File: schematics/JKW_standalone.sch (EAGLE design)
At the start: 229 parts, among them IC1 4093D, IC4 ATMEGA2560-16AU, Q1 BSS84, Q10 BSS84, Q11 BSS84, Q2 BSS84, Q3 BSS84, Q4 BSS84, Q5 BSS84, Q6 BSS84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

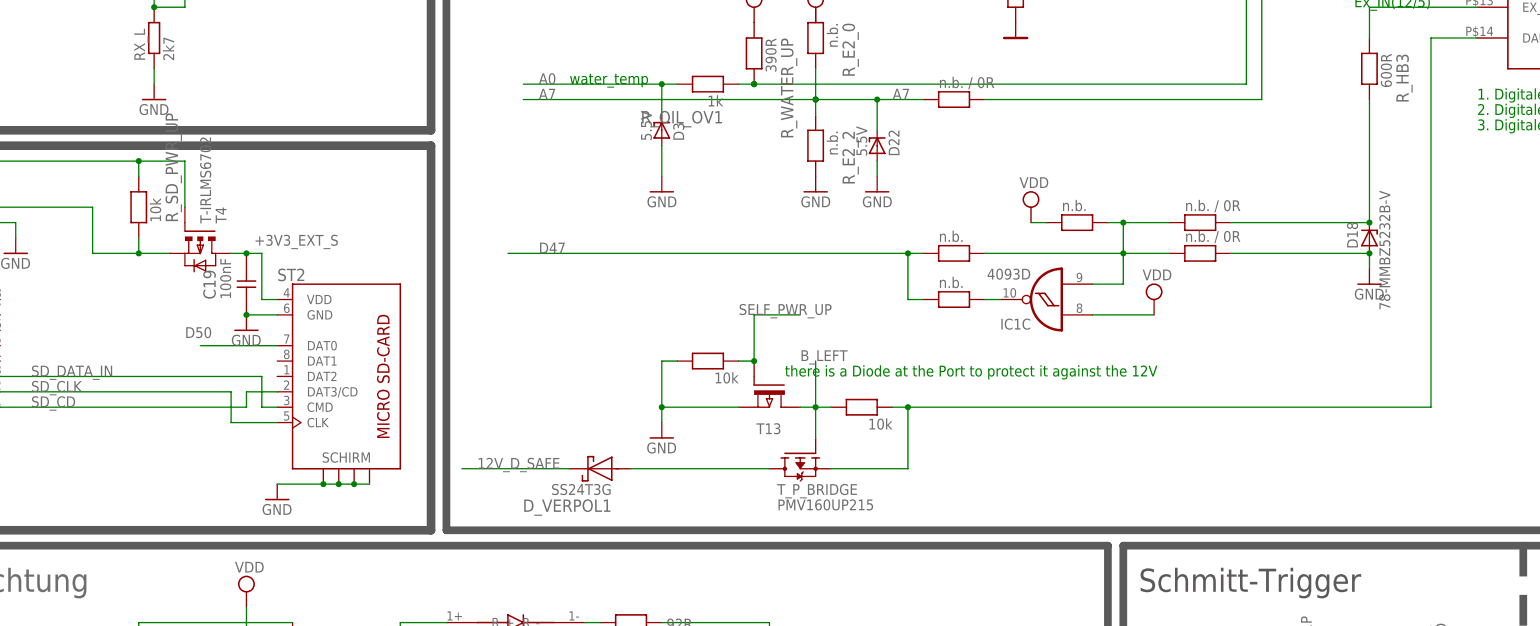
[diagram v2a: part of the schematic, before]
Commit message: improved wiring
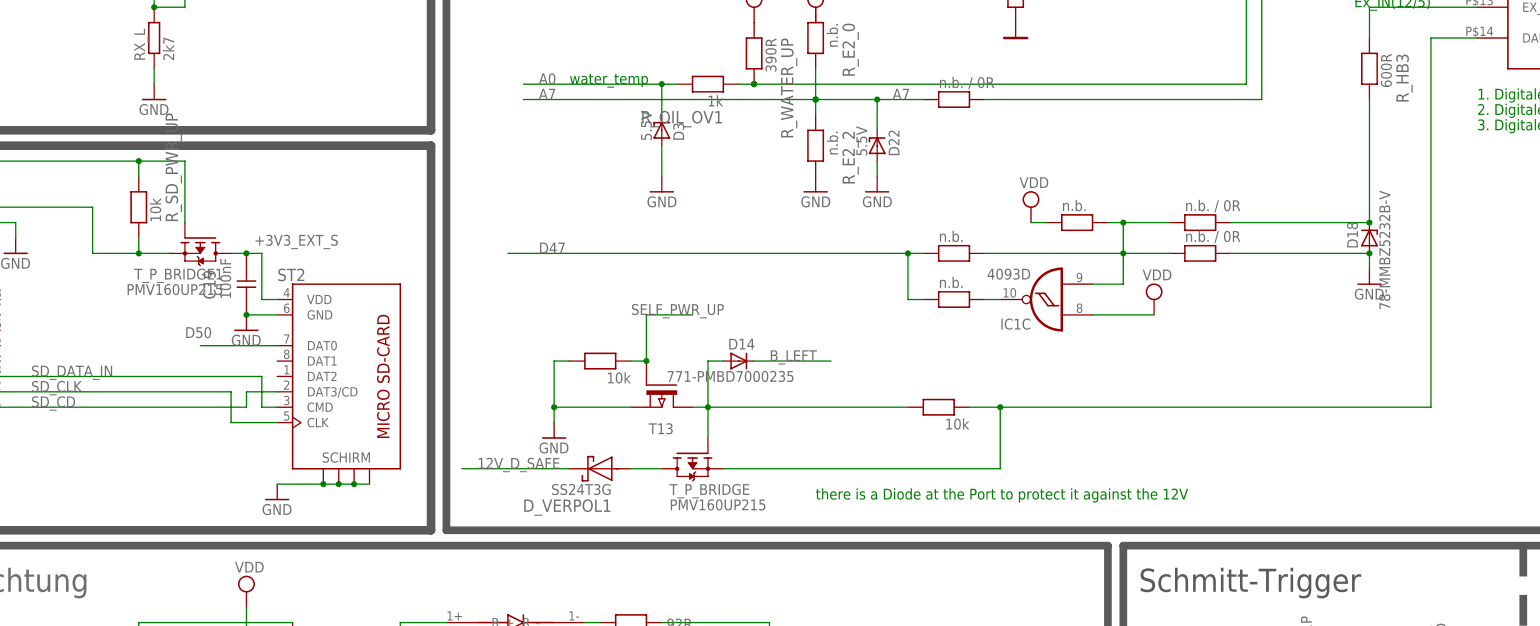
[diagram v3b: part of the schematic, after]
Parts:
- removed T4: T-IRLMS6702, RCLDT:T-IRLMS6702
- added D14: 771-PMBD7000235, semicon-smd-ipc:D-A1-C3
- added T_P_BRIDGE1: PMV160UP215, Kolja:PMV160UP215
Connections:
- new net NET12: D14.A, R_DEAKT_DAUER_P.2, T13.D, T_P_BRIDGE.G
- net +3V3_EXT: now also T_P_BRIDGE1.S; no longer T4.S
- net +3V3_EXT_S: now also T_P_BRIDGE1.D; no longer T4.D1, T4.D2, T4.D3, T4.D4
- net B_LEFT: now also D14.C; no longer R_DEAKT_DAUER_P.2, T13.D, T_P_BRIDGE.G
- net D4: now also T_P_BRIDGE1.G; no longer T4.G
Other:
- moved on the sheet: T13, T_P_BRIDGE
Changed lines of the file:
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@@
 <part name="R_TX_UP" library="RCLDT" deviceset="R" device="0805" value="1k2"/>
 <part name="JP2" library="pinhead" deviceset="PINHD-2X3" device="" value="ICSP"/>
-<part name="T4" library="RCLDT" deviceset="T-IRLMS6702" device=""/>
 <part name="T5" library="RCLDT" deviceset="T-P-FET" device="BSS139" value="Mouser: 771-2N7002BK215 , N-Channel, 60V 350mA, SOT-23, 0,052€"/>
 <part name="GND10" library="supply1" deviceset="GND" device=""/>
@@
 <part name="T_P_BRIDGE" library="Kolja" deviceset="PMV160UP215" device=""/>
 <part name="TX2" library="pinhead" deviceset="PINHD-1X2" device=""/>
+<part name="T_P_BRIDGE1" library="Kolja" deviceset="PMV160UP215" device=""/>
+<part name="D14" library="semicon-smd-ipc" deviceset="D-" device="A1-C3" value="771-PMBD7000235"/>
 </parts>
 <sheets>
@@
 <text x="-137.16" y="-15.24" size="1.778" layer="91">Bluetooth toggle</text>
 <text x="-144.78" y="-20.32" size="1.778" layer="91">V meas</text>
-<text x="71.12" y="91.44" size="1.778" layer="91">there is a Diode at the Port to protect it against the 12V</text>
+<text x="76.2" y="71.12" size="1.778" layer="91">there is a Diode at the Port to protect it against the 12V</text>
 </plain>
 <instances>
@@
 </instance>
 <instance part="JP2" gate="A" x="-132.08" y="38.1" rot="R90"/>
-<instance part="T4" gate="G$1" x="-25.4" y="114.3" rot="MR270"/>
 <instance part="T5" gate="G$1" x="274.32" y="111.76" rot="MR270"/>
 <instance part="GND10" gate="1" x="358.14" y="226.06"/>
@@
 <attribute name="VALUE" x="42.545" y="73.66" size="1.778" layer="96" rot="R180"/>
 </instance>
-<instance part="R_DEAKT_DAUER_P" gate="G$1" x="83.82" y="86.36" smashed="yes" rot="R180">
-<attribute name="VALUE" x="88.9" y="84.455" size="1.778" layer="96" rot="R180"/>
+<instance part="R_DEAKT_DAUER_P" gate="G$1" x="96.52" y="86.36" smashed="yes" rot="R180">
+<attribute name="VALUE" x="101.6" y="84.455" size="1.778" layer="96" rot="R180"/>
 </instance>
-<instance part="T13" gate="G$1" x="68.58" y="88.9" smashed="yes" rot="MR270">
-<attribute name="NAME" x="66.421" y="81.915" size="1.778" layer="95"/>
+<instance part="T13" gate="G$1" x="50.8" y="88.9" smashed="yes" rot="MR270">
+<attribute name="NAME" x="48.641" y="81.915" size="1.778" layer="95"/>
 </instance>
-<instance part="GND15" gate="1" x="50.8" y="81.28"/>
-<instance part="R_DEAKT_DAUER_P1" gate="G$1" x="58.42" y="93.98" smashed="yes" rot="R180">
-<attribute name="VALUE" x="63.5" y="92.075" size="1.778" layer="96" rot="R180"/>
+<instance part="GND15" gate="1" x="33.02" y="81.28"/>
+<instance part="R_DEAKT_DAUER_P1" gate="G$1" x="40.64" y="93.98" smashed="yes" rot="R180">
+<attribute name="VALUE" x="45.72" y="92.075" size="1.778" layer="96" rot="R180"/>
 </instance>
 <instance part="D12" gate="G$1" x="-261.62" y="121.92" smashed="yes" rot="R180"/>
-<instance part="T_P_BRIDGE" gate="G$1" x="73.66" y="78.74" smashed="yes" rot="MR270">
-<attribute name="VALUE" x="69.85" y="71.12" size="1.778" layer="96" rot="MR180"/>
-<attribute name="NAME" x="69.85" y="73.66" size="1.778" layer="95" rot="MR180"/>
+<instance part="T_P_BRIDGE" gate="G$1" x="55.88" y="78.74" smashed="yes" rot="MR270">
+<attribute name="VALUE" x="52.07" y="71.12" size="1.778" layer="96" rot="MR180"/>
+<attribute name="NAME" x="52.07" y="73.66" size="1.778" layer="95" rot="MR180"/>
 </instance>
 <instance part="TX2" gate="G$1" x="-287.02" y="144.78"/>
+<instance part="T_P_BRIDGE1" gate="G$1" x="-25.4" y="114.3" smashed="yes" rot="R270">
+<attribute name="VALUE" x="-21.59" y="106.68" size="1.778" layer="96" rot="R180"/>
+<attribute name="NAME" x="-21.59" y="109.22" size="1.778" layer="95" rot="R180"/>
+</instance>
+<instance part="D14" gate="G$1" x="63.5" y="93.98" smashed="yes">
+<attribute name="NAME" x="61.722" y="95.885" size="1.778" layer="95"/>
+<attribute name="VALUE" x="51.562" y="90.551" size="1.778" layer="96"/>
+</instance>
 </instances>
 <busses>
@@
 <pinref part="GND15" gate="1" pin="GND"/>
 <pinref part="T13" gate="G$1" pin="S"/>
-<wire x1="50.8" y1="83.82" x2="50.8" y2="86.36" width="0.1524" layer="91"/>
-<wire x1="50.8" y1="86.36" x2="63.5" y2="86.36" width="0.1524" layer="91"/>
+<wire x1="33.02" y1="83.82" x2="33.02" y2="86.36" width="0.1524" layer="91"/>
+<wire x1="33.02" y1="86.36" x2="45.72" y2="86.36" width="0.1524" layer="91"/>
 <pinref part="R_DEAKT_DAUER_P1" gate="G$1" pin="2"/>
-<wire x1="50.8" y1="86.36" x2="50.8" y2="93.98" width="0.1524" layer="91"/>
-<wire x1="50.8" y1="93.98" x2="53.34" y2="93.98" width="0.1524" layer="91"/>
-<junction x="50.8" y="86.36"/>
+<wire x1="33.02" y1="86.36" x2="33.02" y2="93.98" width="0.1524" layer="91"/>
+<wire x1="33.02" y1="93.98" x2="35.56" y2="93.98" width="0.1524" layer="91"/>
+<junction x="33.02" y="86.36"/>
 </segment>
 </net>
@@
 <wire x1="-35.56" y1="114.3" x2="-35.56" y2="111.76" width="0.1524" layer="91"/>
 <junction x="-35.56" y="111.76"/>
-<pinref part="T4" gate="G$1" pin="S"/>
 <pinref part="R_SD_PWR_UP" gate="G$1" pin="1"/>
 <wire x1="-43.18" y1="111.76" x2="-43.18" y2="119.38" width="0.1524" layer="91"/>
@@
 <wire x1="-71.12" y1="119.38" x2="-71.12" y2="116.84" width="0.1524" layer="91"/>
 <wire x1="-71.12" y1="116.84" x2="-73.66" y2="116.84" width="0.1524" layer="91"/>
+<pinref part="T_P_BRIDGE1" gate="G$1" pin="S"/>
 </segment>
 </net>
@@
 </segment>
 <segment>
-<wire x1="-27.94" y1="119.38" x2="-27.94" y2="127" width="0.1524" layer="91"/>
+<wire x1="-27.94" y1="116.84" x2="-27.94" y2="127" width="0.1524" layer="91"/>
 <wire x1="-27.94" y1="127" x2="-35.56" y2="127" width="0.1524" layer="91"/>
 <wire x1="-35.56" y1="127" x2="-86.36" y2="127" width="0.1524" layer="91"/>
@@
 <junction x="-35.56" y="127"/>
 <label x="-86.36" y="127" size="1.778" layer="95"/>
-<pinref part="T4" gate="G$1" pin="G"/>
 <pinref part="R_SD_PWR_UP" gate="G$1" pin="2"/>
+<pinref part="T_P_BRIDGE1" gate="G$1" pin="G"/>
 </segment>
 </net>
@@
 <pinref part="ST2" gate="G$1" pin="VDD"/>
 <pinref part="C19" gate="C" pin="2"/>
-<pinref part="T4" gate="G$1" pin="D1"/>
-<pinref part="T4" gate="G$1" pin="D2"/>
-<pinref part="T4" gate="G$1" pin="D3"/>
-<pinref part="T4" gate="G$1" pin="D4"/>
+<pinref part="T_P_BRIDGE1" gate="G$1" pin="D"/>
 </segment>
 </net>
@@
 </segment>
 <segment>
-<wire x1="76.2" y1="93.98" x2="76.2" y2="86.36" width="0.1524" layer="91"/>
-<label x="73.66" y="93.98" size="1.778" layer="95"/>
-<wire x1="78.74" y1="86.36" x2="76.2" y2="86.36" width="0.1524" layer="91"/>
-<wire x1="76.2" y1="86.36" x2="76.2" y2="81.28" width="0.1524" layer="91"/>
-<pinref part="R_DEAKT_DAUER_P" gate="G$1" pin="2"/>
-<wire x1="76.2" y1="86.36" x2="73.66" y2="86.36" width="0.1524" layer="91"/>
-<junction x="76.2" y="86.36"/>
-<pinref part="T13" gate="G$1" pin="D"/>
-<pinref part="T_P_BRIDGE" gate="G$1" pin="G"/>
-</segment>
-<segment>
 <pinref part="D12" gate="G$1" pin="C"/>
 <wire x1="-264.16" y1="121.92" x2="-274.32" y2="121.92" width="0.1524" layer="91"/>
 <label x="-271.78" y="121.92" size="1.778" layer="95"/>
 </segment>
+<segment>
+<pinref part="D14" gate="G$1" pin="C"/>
+<wire x1="66.04" y1="93.98" x2="78.74" y2="93.98" width="0.1524" layer="91"/>
+<label x="68.58" y="93.98" size="1.778" layer="95"/>
+</segment>
 </net>
 <net name="B_UP" class="0">
@@
 <pinref part="SPEEDOSTECKER" gate="G$1" pin="DAUER_VIN"/>
 <wire x1="185.42" y1="147.32" x2="177.8" y2="147.32" width="0.1524" layer="91"/>
-<wire x1="78.74" y1="76.2" x2="91.44" y2="76.2" width="0.1524" layer="91"/>
-<wire x1="91.44" y1="76.2" x2="91.44" y2="86.36" width="0.1524" layer="91"/>
+<wire x1="60.96" y1="76.2" x2="106.68" y2="76.2" width="0.1524" layer="91"/>
+<wire x1="106.68" y1="76.2" x2="106.68" y2="86.36" width="0.1524" layer="91"/>
 <pinref part="R_DEAKT_DAUER_P" gate="G$1" pin="1"/>
-<wire x1="88.9" y1="86.36" x2="91.44" y2="86.36" width="0.1524" layer="91"/>
-<junction x="91.44" y="86.36"/>
-<wire x1="91.44" y1="86.36" x2="177.8" y2="86.36" width="0.1524" layer="91"/>
+<wire x1="101.6" y1="86.36" x2="106.68" y2="86.36" width="0.1524" layer="91"/>
+<junction x="106.68" y="86.36"/>
+<wire x1="106.68" y1="86.36" x2="177.8" y2="86.36" width="0.1524" layer="91"/>
 <wire x1="177.8" y1="86.36" x2="177.8" y2="147.32" width="0.1524" layer="91"/>
 <pinref part="T_P_BRIDGE" gate="G$1" pin="S"/>
@@
 <segment>
 <pinref part="D_VERPOL1" gate="G$1" pin="A"/>
-<wire x1="68.58" y1="76.2" x2="45.72" y2="76.2" width="0.1524" layer="91"/>
+<wire x1="50.8" y1="76.2" x2="45.72" y2="76.2" width="0.1524" layer="91"/>
 <pinref part="T_P_BRIDGE" gate="G$1" pin="D"/>
 </segment>
@@
 <pinref part="T13" gate="G$1" pin="G"/>
 <pinref part="R_DEAKT_DAUER_P1" gate="G$1" pin="1"/>
-<wire x1="66.04" y1="93.98" x2="63.5" y2="93.98" width="0.1524" layer="91"/>
-<wire x1="66.04" y1="93.98" x2="66.04" y2="101.6" width="0.1524" layer="91"/>
-<wire x1="66.04" y1="101.6" x2="73.66" y2="101.6" width="0.1524" layer="91"/>
-<junction x="66.04" y="93.98"/>
-<label x="63.5" y="101.6" size="1.778" layer="95"/>
+<wire x1="48.26" y1="93.98" x2="45.72" y2="93.98" width="0.1524" layer="91"/>
+<wire x1="48.26" y1="93.98" x2="48.26" y2="101.6" width="0.1524" layer="91"/>
+<wire x1="48.26" y1="101.6" x2="55.88" y2="101.6" width="0.1524" layer="91"/>
+<junction x="48.26" y="93.98"/>
+<label x="45.72" y="101.6" size="1.778" layer="95"/>
 </segment>
 <segment>
@@
 </segment>
 </net>
+<net name="NET12" class="0">
+<segment>
+<wire x1="58.42" y1="93.98" x2="58.42" y2="86.36" width="0.1524" layer="91"/>
+<wire x1="91.44" y1="86.36" x2="58.42" y2="86.36" width="0.1524" layer="91"/>
+<wire x1="58.42" y1="86.36" x2="58.42" y2="81.28" width="0.1524" layer="91"/>
+<pinref part="R_DEAKT_DAUER_P" gate="G$1" pin="2"/>
+<wire x1="58.42" y1="86.36" x2="55.88" y2="86.36" width="0.1524" layer="91"/>
+<junction x="58.42" y="86.36"/>
+<pinref part="T13" gate="G$1" pin="D"/>
+<pinref part="T_P_BRIDGE" gate="G$1" pin="G"/>
+<pinref part="D14" gate="G$1" pin="A"/>
+<wire x1="60.96" y1="93.98" x2="58.42" y2="93.98" width="0.1524" layer="91"/>
+</segment>
+</net>

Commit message: Added Capacitor to Display and sandboxed HF-Parts
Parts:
- added C10, C12, C13, GPS_C5: 100nF, RCLDT:C0805
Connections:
- net +3V3_EXT: now also C10.2, C12.2, C13.2, GPS_C5.2
- net GND: now also C10.1, C12.1, C13.1, GPS_C5.1
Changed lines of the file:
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@@
 <?xml version="1.0" encoding="utf-8"?>
 <!DOCTYPE eagle SYSTEM "eagle.dtd">
-<eagle version="6.2">
+<eagle version="6.1">
 <drawing>
 <settings>
@@
 <part name="T_P_BRIDGE1" library="Kolja" deviceset="PMV160UP215" device=""/>
 <part name="D14" library="semicon-smd-ipc" deviceset="D-" device="A1-C3" value="771-PMBD7000235"/>
+<part name="GPS_C5" library="RCLDT" deviceset="C" device="0805" value="100nF"/>
+<part name="C10" library="RCLDT" deviceset="C" device="0805" value="100nF"/>
+<part name="C12" library="RCLDT" deviceset="C" device="0805" value="100nF"/>
+<part name="C13" library="RCLDT" deviceset="C" device="0805" value="100nF"/>
 </parts>
 <sheets>
@@
 <attribute name="VALUE" x="51.562" y="90.551" size="1.778" layer="96"/>
 </instance>
+<instance part="GPS_C5" gate="C" x="236.22" y="162.56" smashed="yes" rot="R90">
+<attribute name="NAME" x="238.76" y="165.1" size="2.032" layer="95" rot="R90"/>
+<attribute name="VALUE" x="233.68" y="160.02" size="1.778" layer="96" rot="R90"/>
+</instance>
+<instance part="C10" gate="C" x="-312.42" y="50.8" rot="R270"/>
+<instance part="C12" gate="C" x="-307.34" y="50.8" rot="R270"/>
+<instance part="C13" gate="C" x="-302.26" y="50.8" rot="R270"/>
 </instances>
 <busses>
@@
 <segment>
 <wire x1="-292.1" y1="45.72" x2="-297.18" y2="45.72" width="0.1524" layer="91"/>
-<wire x1="-297.18" y1="45.72" x2="-314.96" y2="45.72" width="0.1524" layer="91"/>
+<wire x1="-297.18" y1="58.42" x2="-302.26" y2="58.42" width="0.1524" layer="91"/>
+<wire x1="-302.26" y1="58.42" x2="-307.34" y2="58.42" width="0.1524" layer="91"/>
+<wire x1="-307.34" y1="58.42" x2="-312.42" y2="58.42" width="0.1524" layer="91"/>
+<wire x1="-312.42" y1="58.42" x2="-314.96" y2="58.42" width="0.1524" layer="91"/>
 <wire x1="-292.1" y1="35.56" x2="-297.18" y2="35.56" width="0.1524" layer="91"/>
 <wire x1="-297.18" y1="35.56" x2="-297.18" y2="45.72" width="0.1524" layer="91"/>
+<wire x1="-297.18" y1="45.72" x2="-297.18" y2="58.42" width="0.1524" layer="91"/>
 <wire x1="-292.1" y1="22.86" x2="-297.18" y2="22.86" width="0.1524" layer="91"/>
 <wire x1="-297.18" y1="22.86" x2="-297.18" y2="33.02" width="0.1524" layer="91"/>
@@
 <junction x="-297.18" y="22.86"/>
 <junction x="-297.18" y="35.56"/>
-<junction x="-297.18" y="45.72"/>
 <junction x="-297.18" y="33.02"/>
-<label x="-309.88" y="45.72" size="1.778" layer="95"/>
+<label x="-309.88" y="58.42" size="1.778" layer="95"/>
 <pinref part="NHD_2.7" gate="G$1" pin="GND"/>
 <pinref part="NHD_2.7" gate="G$1" pin="GND2"/>
@@
 <pinref part="NHD_2.7" gate="G$1" pin="GND10"/>
 <pinref part="NHD_2.7" gate="G$1" pin="GND3"/>
+<junction x="-297.18" y="45.72"/>
+<pinref part="C13" gate="C" pin="1"/>
+<wire x1="-302.26" y1="55.88" x2="-302.26" y2="58.42" width="0.1524" layer="91"/>
+<pinref part="C12" gate="C" pin="1"/>
+<wire x1="-307.34" y1="55.88" x2="-307.34" y2="58.42" width="0.1524" layer="91"/>
+<pinref part="C10" gate="C" pin="1"/>
+<wire x1="-312.42" y1="55.88" x2="-312.42" y2="58.42" width="0.1524" layer="91"/>
+<junction x="-302.26" y="58.42"/>
+<junction x="-307.34" y="58.42"/>
+<junction x="-312.42" y="58.42"/>
 </segment>
 <segment>
@@
 <pinref part="GPS_C1" gate="C" pin="1"/>
 <wire x1="243.84" y1="157.48" x2="243.84" y2="154.94" width="0.1524" layer="91"/>
+<pinref part="GPS_C5" gate="C" pin="1"/>
+<wire x1="236.22" y1="157.48" x2="236.22" y2="154.94" width="0.1524" layer="91"/>
+<wire x1="236.22" y1="154.94" x2="243.84" y2="154.94" width="0.1524" layer="91"/>
+<junction x="243.84" y="154.94"/>
 </segment>
 <segment>
@@
 </segment>
 <segment>
-<wire x1="-292.1" y1="43.18" x2="-314.96" y2="43.18" width="0.1524" layer="91"/>
+<wire x1="-292.1" y1="43.18" x2="-302.26" y2="43.18" width="0.1524" layer="91"/>
 <label x="-309.88" y="43.18" size="1.778" layer="95"/>
 <pinref part="NHD_2.7" gate="G$1" pin="VDD"/>
+<pinref part="C10" gate="C" pin="2"/>
+<wire x1="-302.26" y1="43.18" x2="-307.34" y2="43.18" width="0.1524" layer="91"/>
+<wire x1="-307.34" y1="43.18" x2="-312.42" y2="43.18" width="0.1524" layer="91"/>
+<wire x1="-312.42" y1="43.18" x2="-314.96" y2="43.18" width="0.1524" layer="91"/>
+<wire x1="-312.42" y1="45.72" x2="-312.42" y2="43.18" width="0.1524" layer="91"/>
+<pinref part="C12" gate="C" pin="2"/>
+<wire x1="-307.34" y1="45.72" x2="-307.34" y2="43.18" width="0.1524" layer="91"/>
+<pinref part="C13" gate="C" pin="2"/>
+<wire x1="-302.26" y1="45.72" x2="-302.26" y2="43.18" width="0.1524" layer="91"/>
+<junction x="-312.42" y="43.18"/>
+<junction x="-307.34" y="43.18"/>
+<junction x="-302.26" y="43.18"/>
 </segment>
 <segment>
@@
 <wire x1="287.02" y1="167.64" x2="287.02" y2="170.18" width="0.1524" layer="91"/>
 <wire x1="287.02" y1="170.18" x2="243.84" y2="170.18" width="0.1524" layer="91"/>
-<wire x1="243.84" y1="170.18" x2="231.14" y2="170.18" width="0.1524" layer="91"/>
+<wire x1="243.84" y1="170.18" x2="236.22" y2="170.18" width="0.1524" layer="91"/>
+<wire x1="236.22" y1="170.18" x2="231.14" y2="170.18" width="0.1524" layer="91"/>
 <wire x1="243.84" y1="167.64" x2="243.84" y2="170.18" width="0.1524" layer="91"/>
 <junction x="287.02" y="170.18"/>
@@
 <pinref part="GPS" gate="G$1" pin="EN"/>
 <pinref part="GPS_C1" gate="C" pin="2"/>
+<pinref part="GPS_C5" gate="C" pin="2"/>
+<wire x1="236.22" y1="167.64" x2="236.22" y2="170.18" width="0.1524" layer="91"/>
+<junction x="236.22" y="170.18"/>
 </segment>
 <segment>
@@
 </segment>
 <segment>
-<wire x1="-25.4" y1="96.52" x2="-12.7" y2="96.52" width="0.1524" layer="91"/>
-<label x="-27.94" y="97.79" size="1.778" layer="95"/>
+<wire x1="-40.64" y1="96.52" x2="-12.7" y2="96.52" width="0.1524" layer="91"/>
 <pinref part="ST2" gate="G$1" pin="DAT0"/>
-</segment>
-</net>
+<label x="-35.56" y="96.52" size="1.778" layer="95"/>
+</segment>
+</net>
